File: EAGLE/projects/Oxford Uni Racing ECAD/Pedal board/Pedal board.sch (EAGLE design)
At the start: 45 parts, among them IC1 AD711N, J1 ASS + BOTS, J2 THR_1_2, J3 PWR_CAN, J6 BR_POS_PRESS_STWH, K2 EC2-12TNU, T1 BT169, X2 D-SUB9-H2M09ST

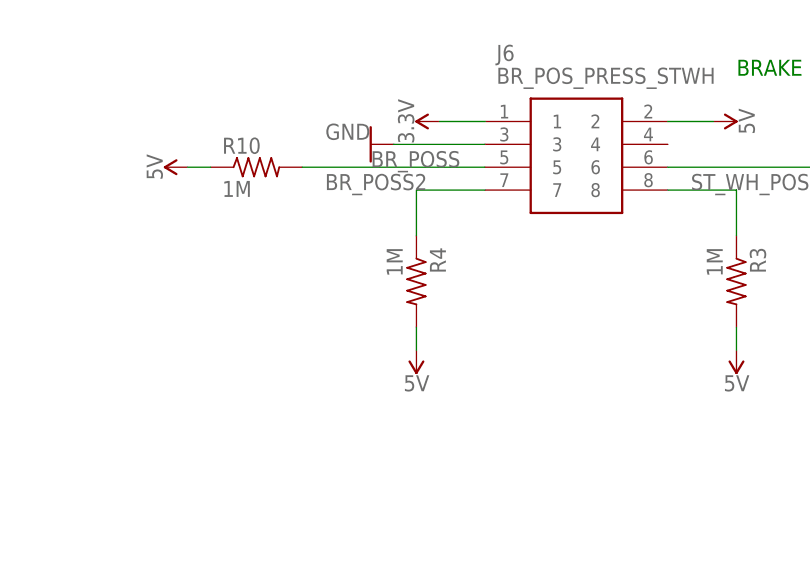
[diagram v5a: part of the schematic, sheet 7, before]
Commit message: removed brake lights from pedal board
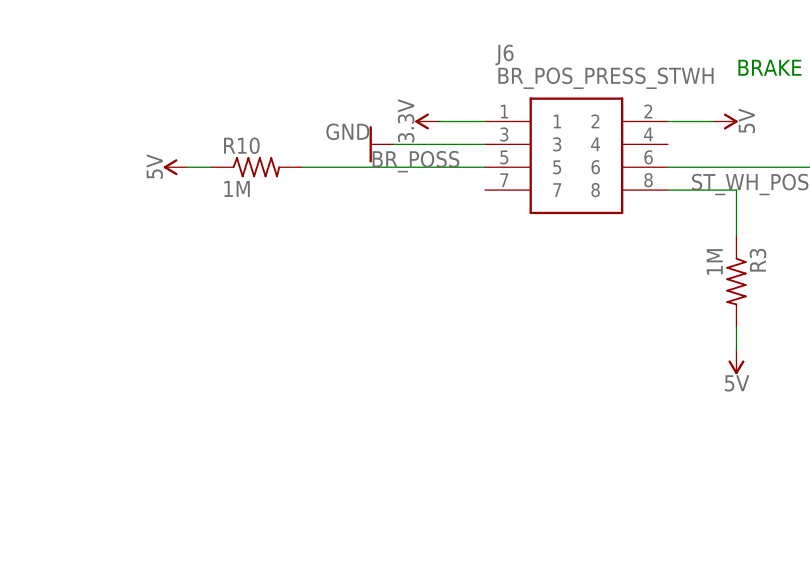
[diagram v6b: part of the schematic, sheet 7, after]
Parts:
- removed R4: 1M, adafruit:R-US_0204/7
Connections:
- removed net BR_POSS2: J6.7, R4.1
- net 5V: no longer R4.2
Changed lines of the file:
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@@
 <part name="R2" library="adafruit" library_urn="urn:adsk.eagle:library:420" deviceset="R-US_" device="0204/7" package3d_urn="urn:adsk.eagle:package:6240596/1" value="1M"/>
 <part name="R3" library="adafruit" library_urn="urn:adsk.eagle:library:420" deviceset="R-US_" device="0204/7" package3d_urn="urn:adsk.eagle:package:6240596/1" value="1M"/>
-<part name="R4" library="adafruit" library_urn="urn:adsk.eagle:library:420" deviceset="R-US_" device="0204/7" package3d_urn="urn:adsk.eagle:package:6240596/1" value="1M"/>
 <part name="R10" library="adafruit" library_urn="urn:adsk.eagle:library:420" deviceset="R-US_" device="0204/7" package3d_urn="urn:adsk.eagle:package:6240596/1" value="1M"/>
 <part name="R11" library="adafruit" library_urn="urn:adsk.eagle:library:420" deviceset="R-US_" device="0204/7" package3d_urn="urn:adsk.eagle:package:6240596/1" value="1M"/>
@@
 <part name="SUPPLY43" library="SparkFun-PowerSymbols" library_urn="urn:adsk.eagle:library:530" deviceset="5V" device=""/>
 <part name="SUPPLY44" library="SparkFun-PowerSymbols" library_urn="urn:adsk.eagle:library:530" deviceset="5V" device=""/>
-<part name="SUPPLY45" library="SparkFun-PowerSymbols" library_urn="urn:adsk.eagle:library:530" deviceset="5V" device=""/>
 <part name="3.3V_IND" library="adafruit" library_urn="urn:adsk.eagle:library:420" deviceset="LED" device="3MM" package3d_urn="urn:adsk.eagle:package:6240537/1"/>
 <part name="R23" library="adafruit" library_urn="urn:adsk.eagle:library:420" deviceset="R-US_" device="0204/7" package3d_urn="urn:adsk.eagle:package:6240596/1"/>
@@
 <attribute name="VALUE" x="166.878" y="31.75" size="1.778" layer="96" rot="R270"/>
 </instance>
-<instance part="R4" gate="G$1" x="134.62" y="27.94" smashed="yes" rot="R270">
-<attribute name="NAME" x="136.1186" y="31.75" size="1.778" layer="95" rot="R270"/>
-<attribute name="VALUE" x="131.318" y="31.75" size="1.778" layer="96" rot="R270"/>
-</instance>
 <instance part="R10" gate="G$1" x="116.84" y="40.64" smashed="yes">
 <attribute name="NAME" x="113.03" y="42.1386" size="1.778" layer="95"/>
@@
 <instance part="SUPPLY44" gate="G$1" x="170.18" y="20.32" smashed="yes" rot="R180">
 <attribute name="VALUE" x="170.18" y="17.526" size="1.778" layer="96" rot="R180" align="bottom-center"/>
-</instance>
-<instance part="SUPPLY45" gate="G$1" x="134.62" y="20.32" smashed="yes" rot="R180">
-<attribute name="VALUE" x="134.62" y="17.526" size="1.778" layer="96" rot="R180" align="bottom-center"/>
 </instance>
 </instances>
@@
 <pinref part="SUPPLY19" gate="G$1" pin="5V"/>
 <wire x1="111.76" y1="40.64" x2="109.22" y2="40.64" width="0.1524" layer="91"/>
-</segment>
-<segment>
-<pinref part="R4" gate="G$1" pin="2"/>
-<pinref part="SUPPLY45" gate="G$1" pin="5V"/>
-<wire x1="134.62" y1="22.86" x2="134.62" y2="20.32" width="0.1524" layer="91"/>
 </segment>
 <segment>
@@
 </segment>
 </net>
-<net name="BR_POSS2" class="0">
-<segment>
-<pinref part="J6" gate="G$1" pin="7"/>
-<label x="124.46" y="38.1" size="1.778" layer="95"/>
-<pinref part="R4" gate="G$1" pin="1"/>
-<wire x1="134.62" y1="33.02" x2="134.62" y2="38.1" width="0.1524" layer="91"/>
-<wire x1="134.62" y1="38.1" x2="142.24" y2="38.1" width="0.1524" layer="91"/>
-</segment>
-</net>

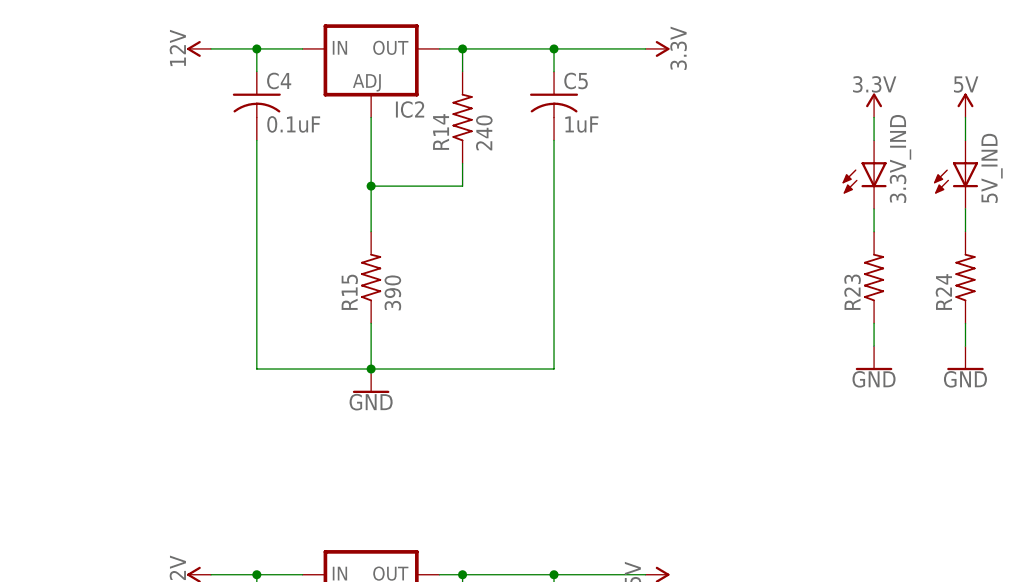
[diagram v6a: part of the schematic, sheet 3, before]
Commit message: removed 3.3V regulators from boards, as we will be using the onbloard regulator
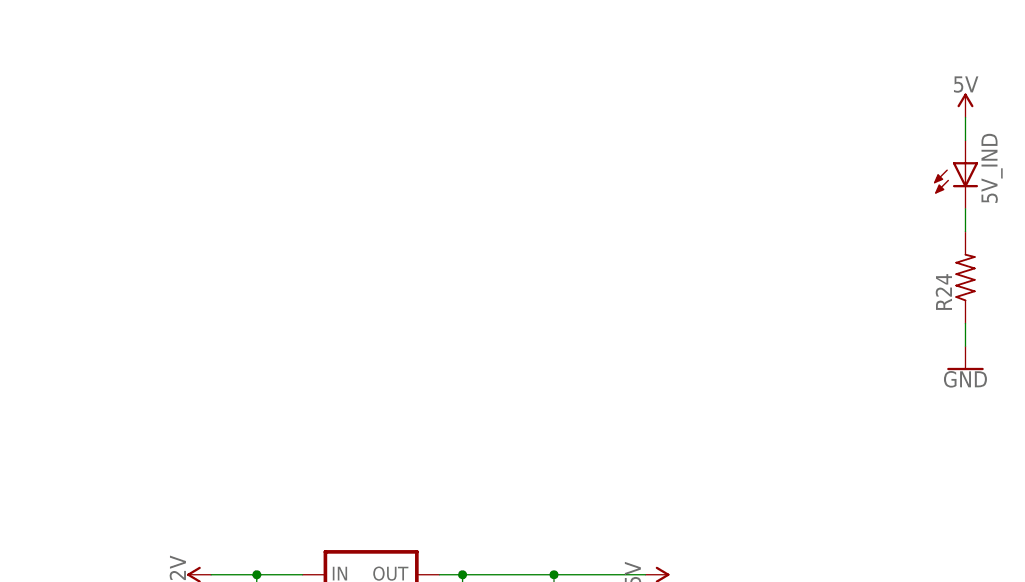
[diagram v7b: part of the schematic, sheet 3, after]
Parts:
- removed 3.3V_IND: (no value), adafruit:LED3MM
- removed C4: 0.1uF, adafruit:C-US050-025X075
- removed C5: 1uF, adafruit:C-US050-025X075
- removed IC2: (no value), v-reg:LM317TS
- removed R14: 240, adafruit:R-US_0204/7
- removed R15: 390, adafruit:R-US_0204/7
- removed R23: (no value), adafruit:R-US_0204/7
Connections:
- removed net N$12: 3.3V_IND.C, R23.2
- removed net N$24: IC2.ADJ, R14.1, R15.2
- net 12V: no longer C4.1, IC2.IN
- net 3.3V: now also U$1.J802-3.3V; no longer 3.3V_IND.A, C5.1, IC2.OUT, R14.2
- net GND: no longer C4.2, C5.2, R15.1, R23.1

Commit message: routed board gor pedal board
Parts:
- R20, R7, R8, R9: device rcl:R-EU_0207/15 -> adafruit:R-US_0204/7
- R5, R6: device rcl:R-EU_0207/15 -> BeagleBone_Black_Wireless:R-US_0207/15
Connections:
- net 12V: now also R21.E
- net 3.3V: now also J6.2; no longer J6.1
- net 5V: now also J6.1, R24.2; no longer 5V_IND.A, J6.2, R21.E
- net ASS2: now also J1.6
- net BATT_CURRENT: now also COMPARATORA.+IN, J6.8; no longer COMPARATORB.+IN, J1.5
- net BR_POSS: now also U$1.J803-4-PB07; no longer U$1.J803-2-PA08
- net BR_PRESS: now also COMPARATORB.+IN, U$1.J803-2-PA08; no longer COMPARATORA.+IN, U$1.J803-4-PB07
- net GND: now also 5V_IND.C; no longer R24.1
- net N$3: now also J1.5
- net N$4: now also 5V_IND.A, R24.1; no longer 5V_IND.C, R24.2
- net ST_WH_POSS: now also J6.7; no longer J6.8
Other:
- note added: "Connect BOTS between pins 7 and 8 Connect RESET button between pins 1 and 2 Connect ASS loop between pins 3,5 and 4,6 (two pins due to high current surges"
- note removed: "Connect BOTS between pins 7 and 8 Connect RESET button between pins 1 and 2 Connect ASS loop between pins 3 and 4 Connect BATT_CURRENT to pin 5"
- moved on the sheet: 5V_IND, R24, R3
